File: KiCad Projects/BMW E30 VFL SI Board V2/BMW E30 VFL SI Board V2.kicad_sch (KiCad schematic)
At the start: 33 parts, among them J2 Conn_01x19_Pin, Q2 BC557B, Q3 BC337-25, Q4 BC547C, U1 ITT SAF MCU, Y1 Crystal

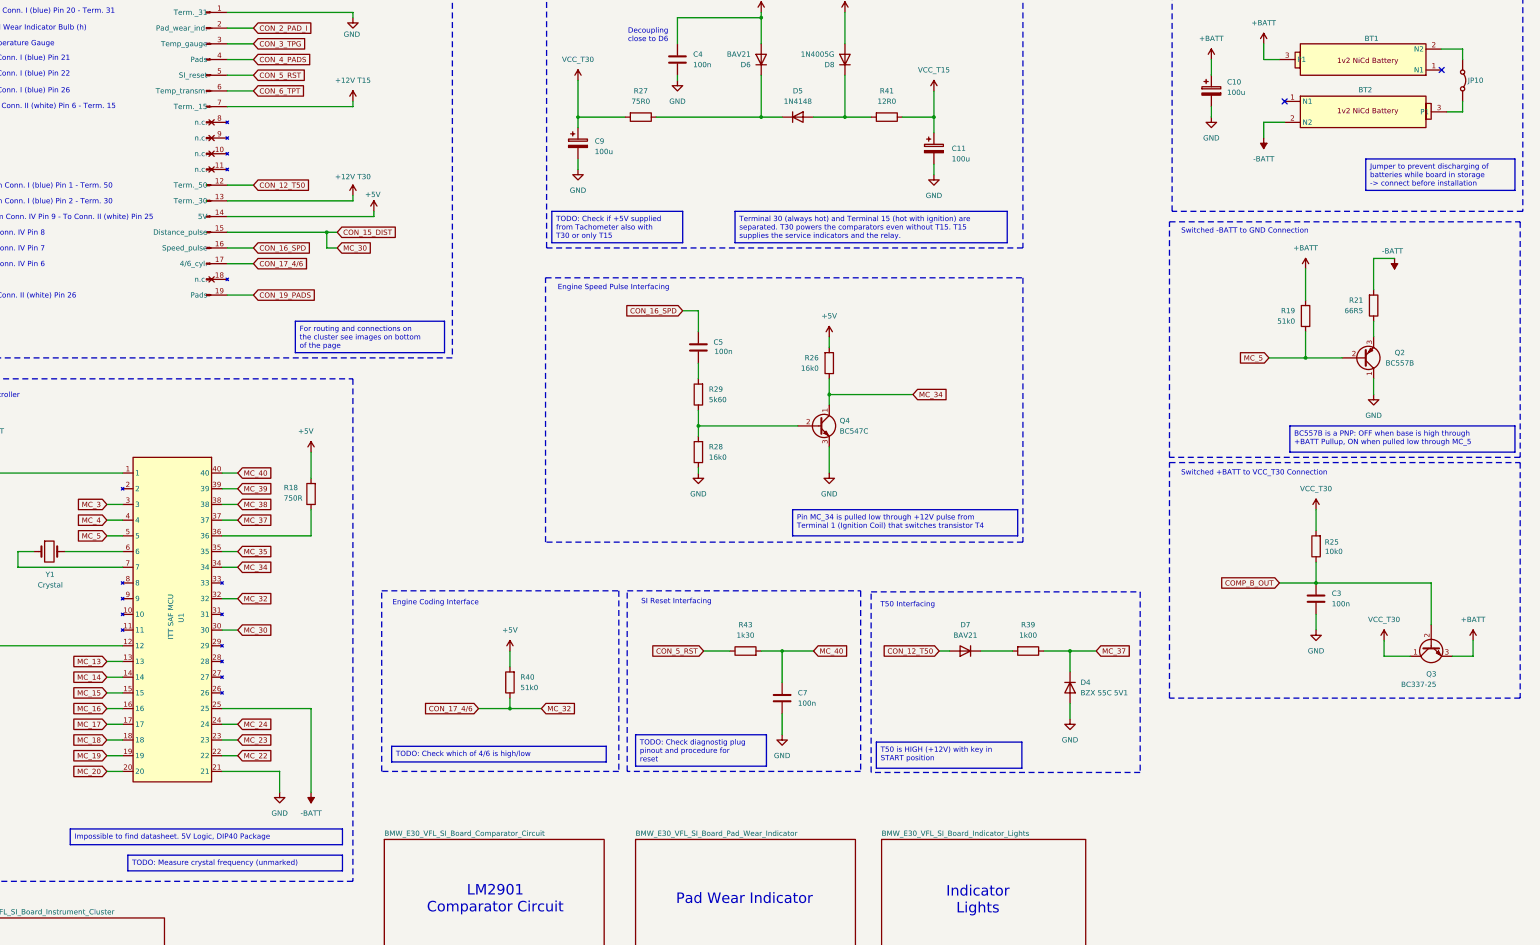
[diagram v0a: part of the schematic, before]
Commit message: V2 Board Updates
Added in extra resistors, cap, and diode that were added to a  particular version of the SI board from the USDM on the comparator circuit. Updated the schematic diagram of the comparator circuit to improve readability. Updated the clock frequency measured with a scope. Made a few minor layout improvements including moving the "JP" connections inwards as not to interfere with the plastic housing for the PCB in the cluster and other minor layout errors such as swapped reference designators. Updated info on where the +5V regulator gets its source voltage from. These updates are reflected in schematic version V2.1 as denoted in the title box (not in the title of the schematic file).
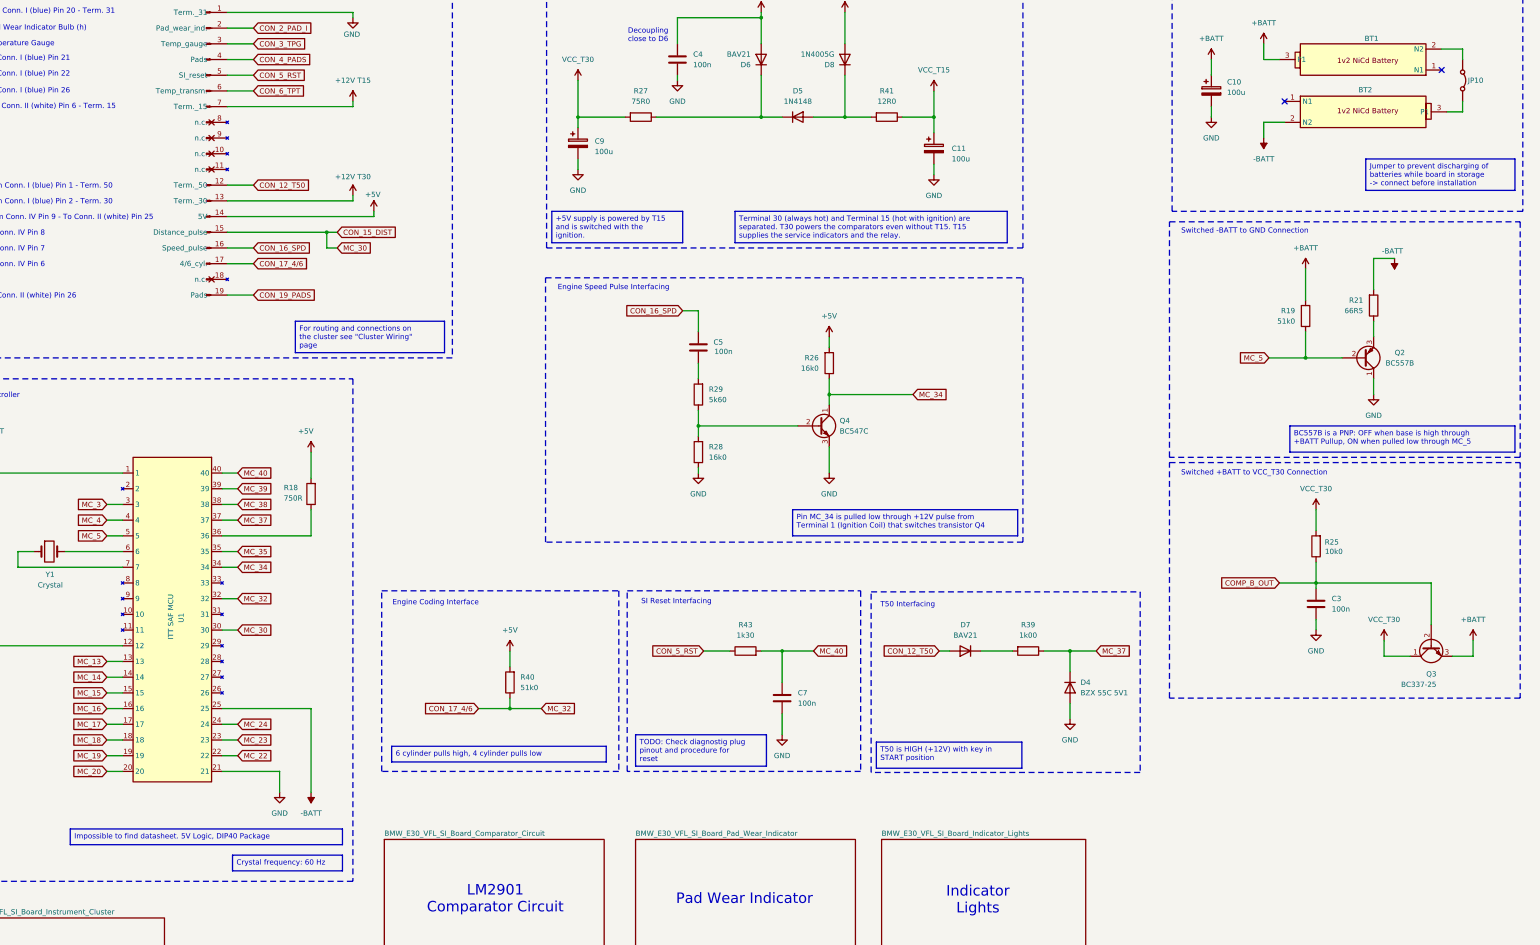
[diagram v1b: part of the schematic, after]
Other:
- moved on the sheet: C3

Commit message: Footprint Change
Changed battery enable jumper footprint to a THT to make changing the connection easier.
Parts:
- JP10: footprint Jumper:SolderJumper-2_P1.3mm_Open_RoundedPad1.0x1.5mm -> Connector_PinHeader_2.54mm:PinHeader_1x02_P2.54mm_Vertical
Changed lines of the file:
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@@
 			)
 		)
-		(property "Footprint" "Jumper:SolderJumper-2_P1.3mm_Open_RoundedPad1.0x1.5mm"
+		(property "Footprint" "Connector_PinHeader_2.54mm:PinHeader_1x02_P2.54mm_Vertical"
 			(at 386.08 48.26 0)
 			(effects

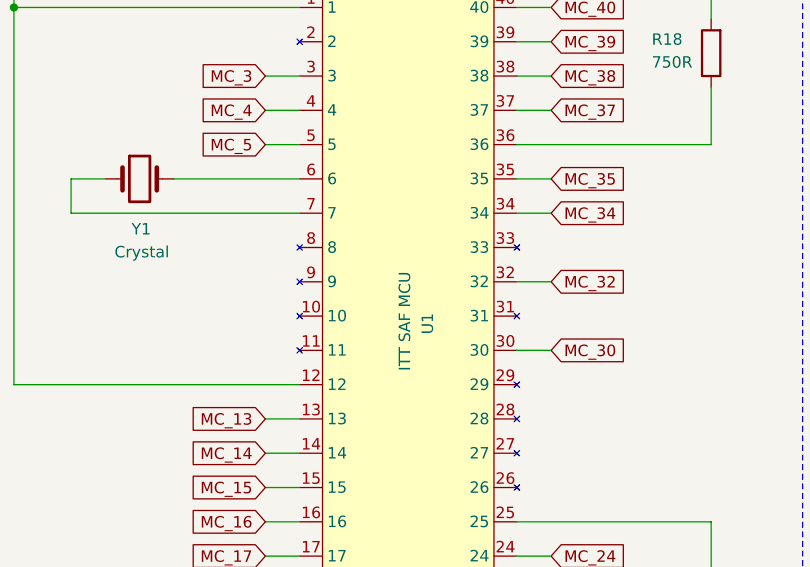
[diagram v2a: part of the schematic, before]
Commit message: Update Name of SAF chip
SAF1093 chip number added.
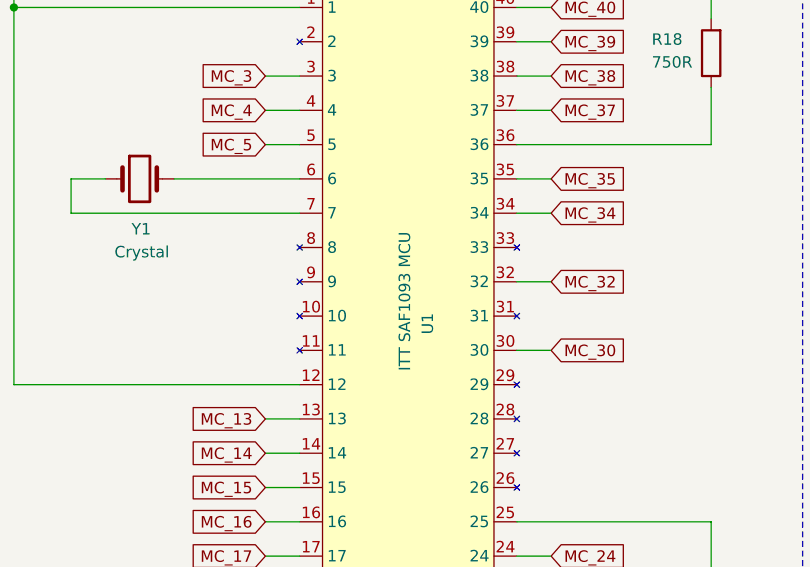
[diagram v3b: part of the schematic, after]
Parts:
- U1: value ITT SAF MCU -> ITT SAF1093 MCU
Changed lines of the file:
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@@
 			)
 		)
-		(property "Value" "ITT SAF MCU"
+		(property "Value" "ITT SAF1093 MCU"
 			(at 72.644 183.896 0)
 			(effects
